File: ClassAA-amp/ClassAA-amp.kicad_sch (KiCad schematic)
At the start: 30 parts, among them J1 XH_3pin, J2 AudioJack3, J3 AudioJack3, U1 NJM4580E, U2 NJM4556

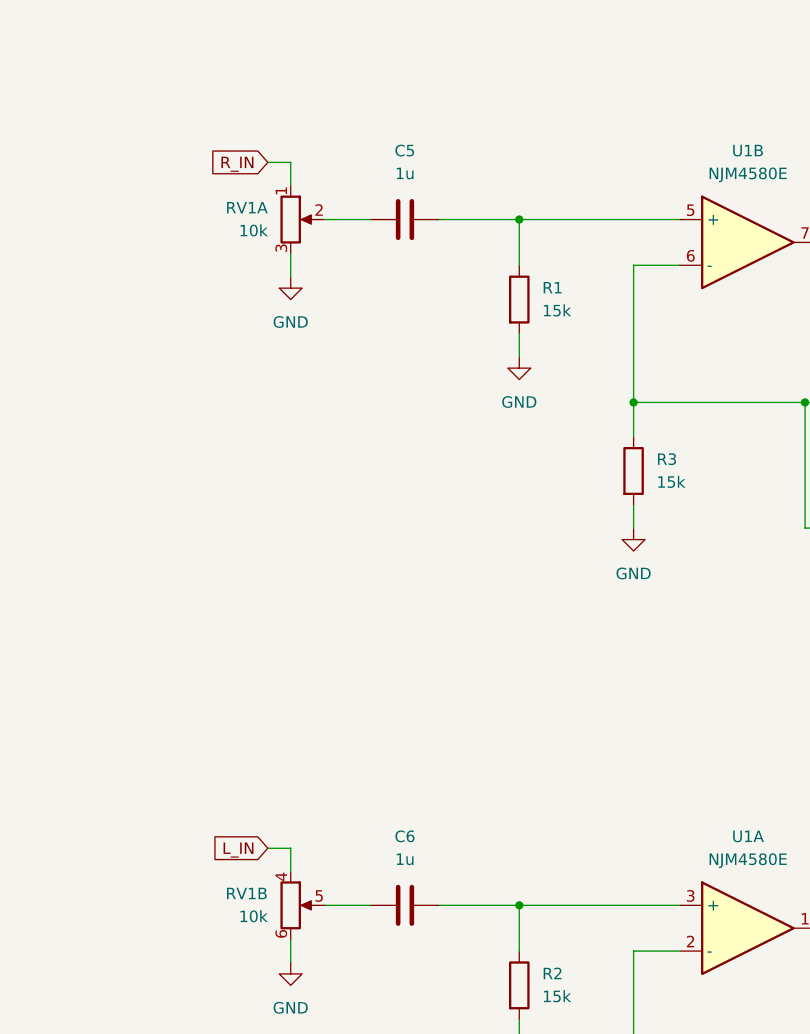
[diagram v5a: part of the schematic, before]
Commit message: 入力ハイパスフィルタのCを10uFに変更
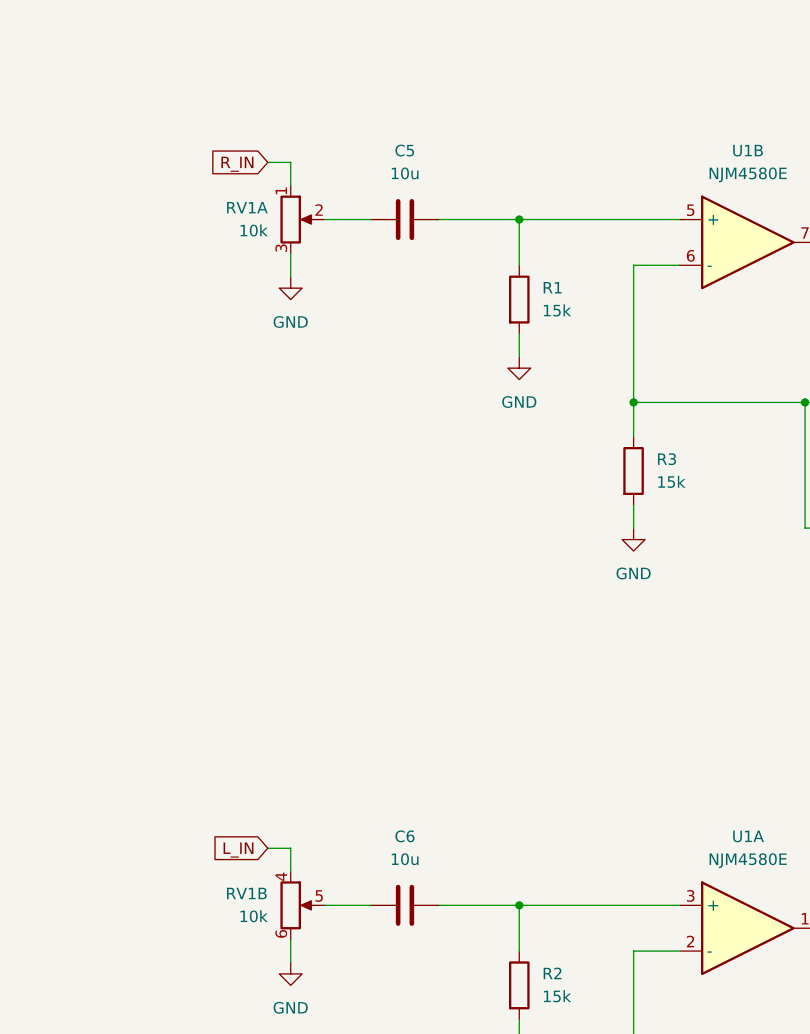
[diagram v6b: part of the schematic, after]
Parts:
- C5, C6: value 1u -> 10u
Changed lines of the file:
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@@
       (effects (font (size 1.27 1.27)))
     )
-    (property "Value" "1u" (at 139.7 119.38 90)
+    (property "Value" "10u" (at 139.7 119.38 90)
       (effects (font (size 1.27 1.27)))
     )
@@
       (effects (font (size 1.27 1.27)))
     )
-    (property "Value" "1u" (at 139.7 43.18 90)
-      (effects (font (size 1.27 1.27)))
-    )
+    (property "Value" "10u" (at 139.7 43.18 90)
+      (effects (font (size 1.27 1.27)))
+    )

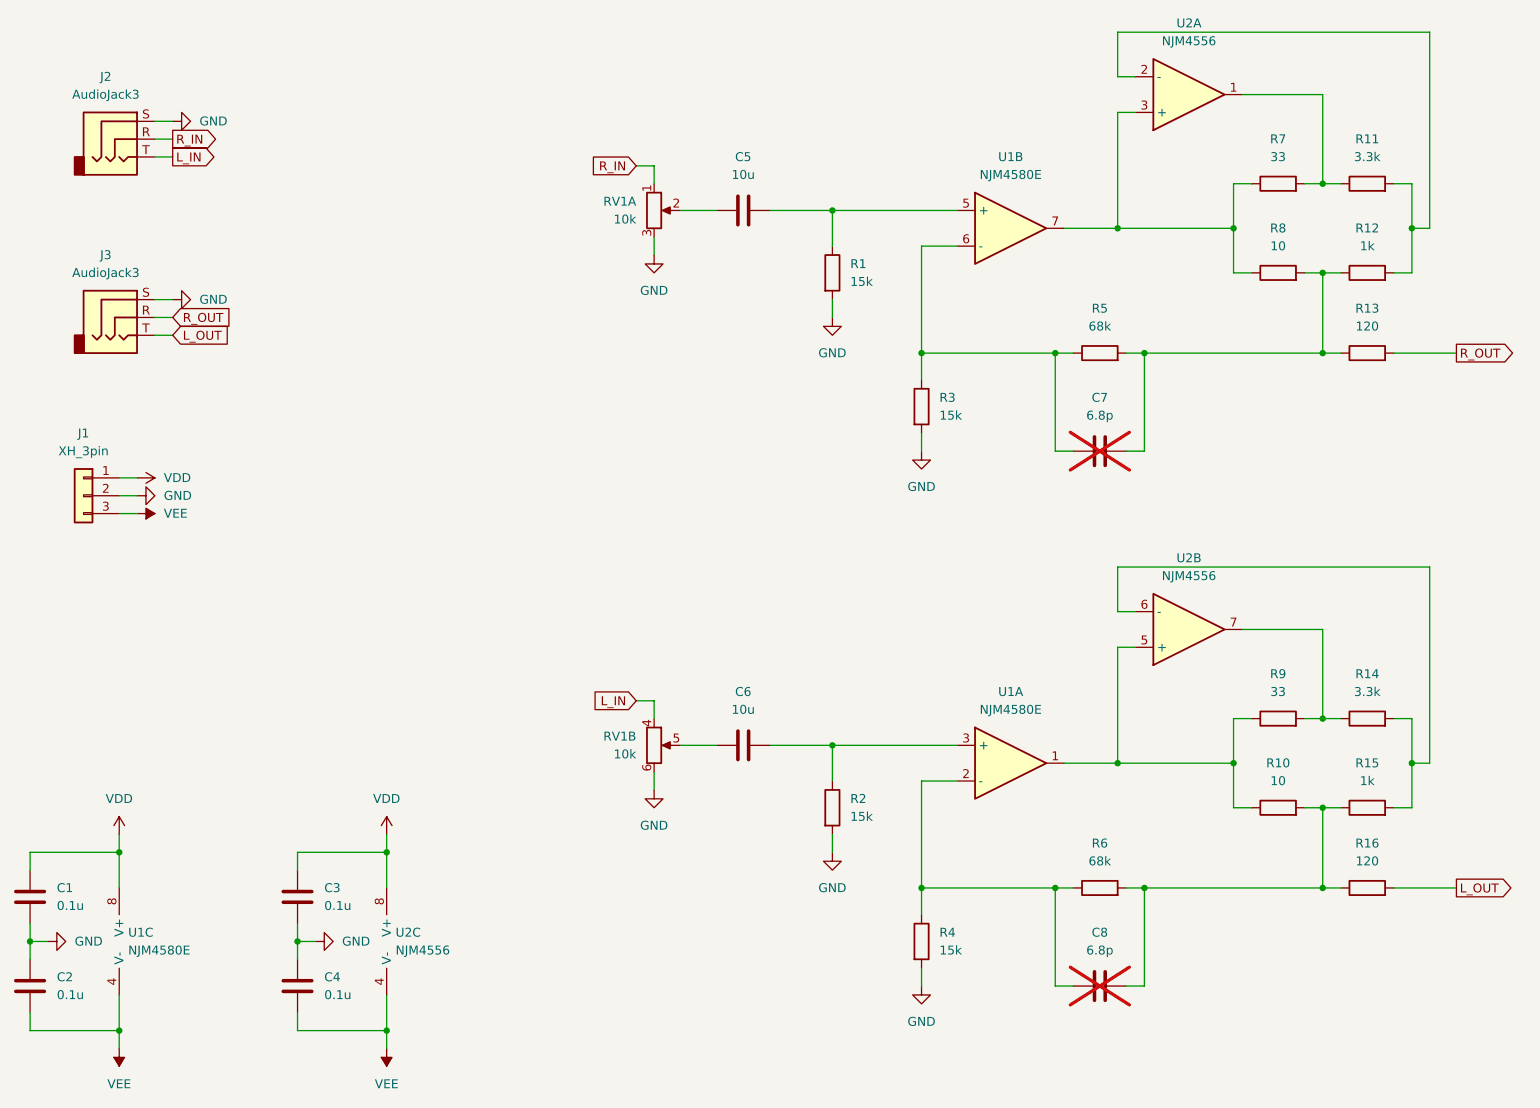
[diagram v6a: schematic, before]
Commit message: オペアンプの型番修正、フットプリント割当
NJM4580DD, NJM4556AD
フットプリントはオーディオジャック以外
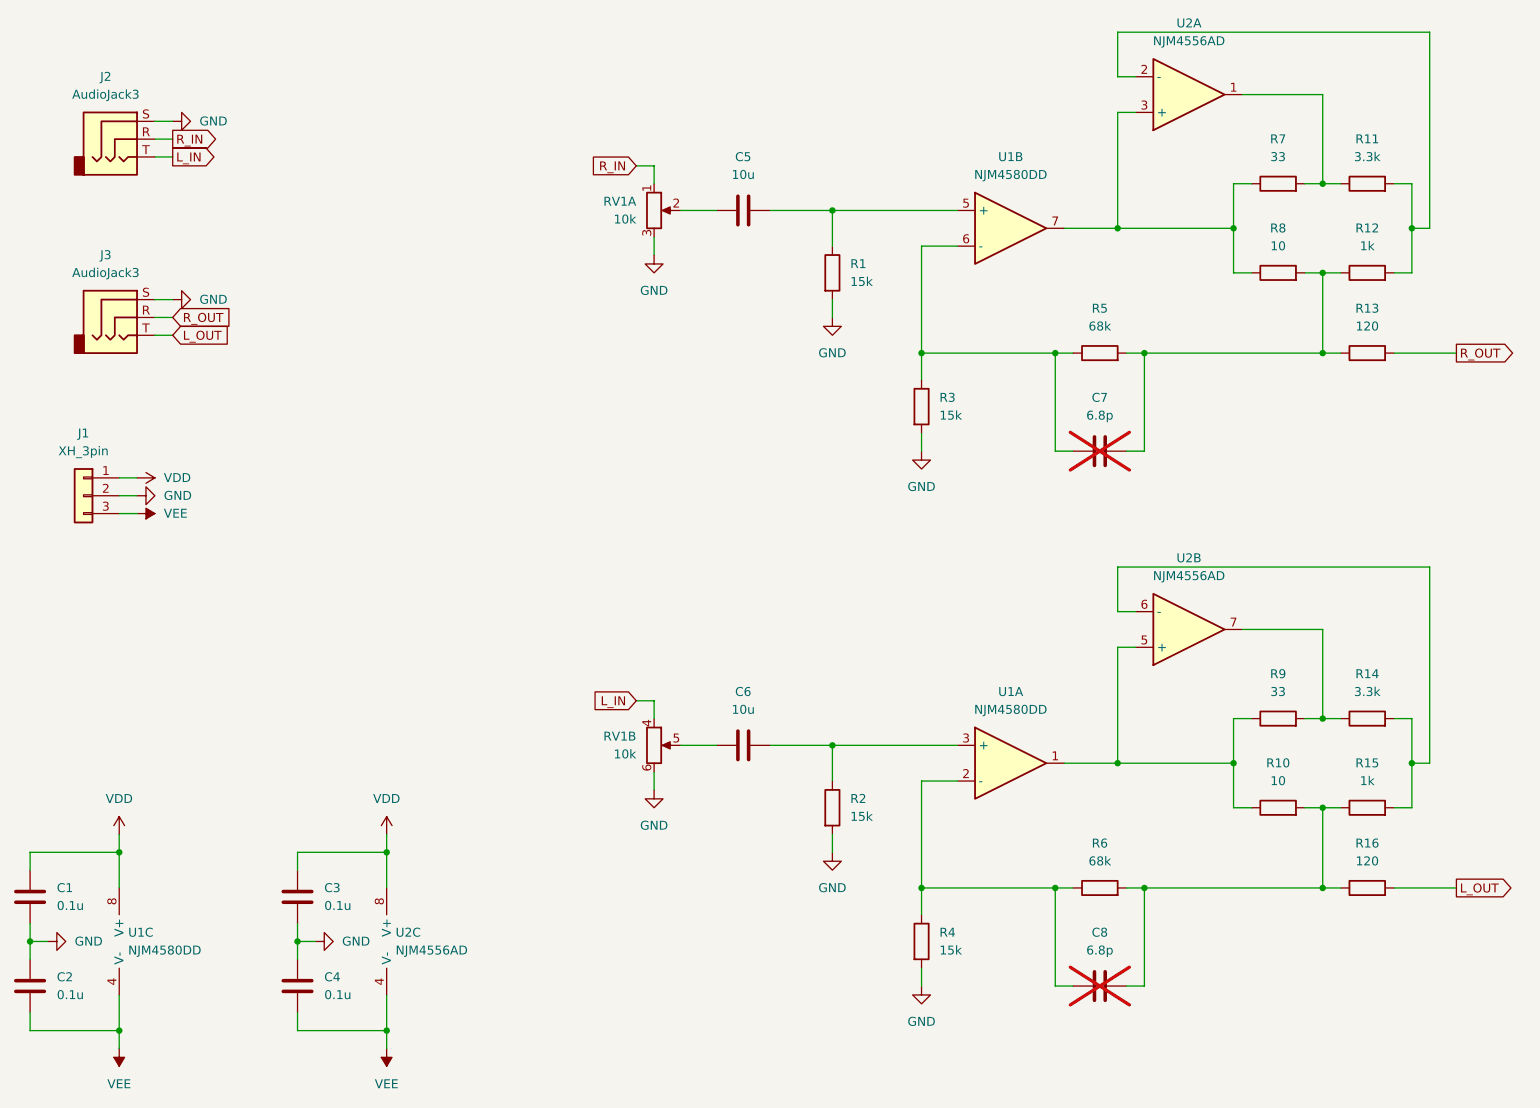
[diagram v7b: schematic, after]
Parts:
- C1, C2, C3, C4, C5, C6: footprint (none) -> Capacitor_SMD:C_0603_1608Metric
- C7, C8: footprint (none) -> Capacitor_SMD:C_0402_1005Metric
- J1: footprint (none) -> Connector_JST:JST_XH_B3B-XH-A_1x03_P2.50mm_Vertical
- R1, R10, R11, R12, R13, R14, R15, R16, R2, R3, R4, R5, R6, R7, R8, R9: footprint (none) -> Resistor_SMD:R_0603_1608Metric
- RV1: footprint (none) -> Potentiometer_THT:Potentiometer_Alps_RK097_Dual_Horizontal
- U1: value NJM4580E -> NJM4580DD; footprint (none) -> Package_DIP:DIP-8_W7.62mm_Socket
- U2: value NJM4556 -> NJM4556AD; footprint (none) -> Package_DIP:DIP-8_W7.62mm_Socket
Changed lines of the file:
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@@
       (effects (font (size 1.27 1.27)))
     )
-    (property "Footprint" "" (at 215.9 58.928 90)
+    (property "Footprint" "Resistor_SMD:R_0603_1608Metric" (at 215.9 58.928 90)
       (effects (font (size 1.27 1.27)) hide)
     )
@@
       (effects (font (size 1.27 1.27)))
     )
-    (property "Footprint" "" (at 228.6 58.928 90)
+    (property "Footprint" "Resistor_SMD:R_0603_1608Metric" (at 228.6 58.928 90)
       (effects (font (size 1.27 1.27)) hide)
     )
@@
       (effects (font (size 1.27 1.27)))
     )
-    (property "Value" "NJM4580E" (at 177.8 119.38 0)
-      (effects (font (size 1.27 1.27)))
-    )
-    (property "Footprint" "" (at 177.8 127 0)
+    (property "Value" "NJM4580DD" (at 177.8 119.38 0)
+      (effects (font (size 1.27 1.27)))
+    )
+    (property "Footprint" "Package_DIP:DIP-8_W7.62mm_Socket" (at 177.8 127 0)
       (effects (font (size 1.27 1.27)) hide)
     )
@@
       (effects (font (size 1.27 1.27)))
     )
-    (property "Footprint" "" (at 228.6 122.428 90)
+    (property "Footprint" "Resistor_SMD:R_0603_1608Metric" (at 228.6 122.428 90)
       (effects (font (size 1.27 1.27)) hide)
     )
@@
       (effects (font (size 1.27 1.27)))
     )
-    (property "Value" "NJM4556" (at 203.2 24.13 0)
-      (effects (font (size 1.27 1.27)))
-    )
-    (property "Footprint" "" (at 203.2 31.75 0)
+    (property "Value" "NJM4556AD" (at 203.2 24.13 0)
+      (effects (font (size 1.27 1.27)))
+    )
+    (property "Footprint" "Package_DIP:DIP-8_W7.62mm_Socket" (at 203.2 31.75 0)
       (effects (font (size 1.27 1.27)) hide)
     )
@@
       (effects (font (size 1.27 1.27)))
     )
-    (property "Value" "NJM4556" (at 203.2 100.33 0)
-      (effects (font (size 1.27 1.27)))
-    )
-    (property "Footprint" "" (at 203.2 107.95 0)
+    (property "Value" "NJM4556AD" (at 203.2 100.33 0)
+      (effects (font (size 1.27 1.27)))
+    )
+    (property "Footprint" "Package_DIP:DIP-8_W7.62mm_Socket" (at 203.2 107.95 0)
       (effects (font (size 1.27 1.27)) hide)
     )
@@
       (effects (font (size 1.27 1.27)) (justify left))
     )
-    (property "Footprint" "" (at 163.322 152.4 90)
+    (property "Footprint" "Resistor_SMD:R_0603_1608Metric" (at 163.322 152.4 90)
       (effects (font (size 1.27 1.27)) hide)
     )
@@
       (effects (font (size 1.27 1.27)) (justify left))
     )
-    (property "Footprint" "" (at 77.1652 149.86 0)
+    (property "Footprint" "Capacitor_SMD:C_0603_1608Metric" (at 77.1652 149.86 0)
       (effects (font (size 1.27 1.27)) hide)
     )
@@
       (effects (font (size 1.27 1.27)))
     )
-    (property "Footprint" "" (at 143.51 123.4948 0)
+    (property "Footprint" "Capacitor_SMD:C_0603_1608Metric" (at 143.51 123.4948 0)
       (effects (font (size 1.27 1.27)) hide)
     )
@@
       (effects (font (size 1.27 1.27)) (justify left))
     )
-    (property "Value" "NJM4556" (at 90.17 153.67 0)
-      (effects (font (size 1.27 1.27)) (justify left))
-    )
-    (property "Footprint" "" (at 91.44 152.4 0)
+    (property "Value" "NJM4556AD" (at 90.17 153.67 0)
+      (effects (font (size 1.27 1.27)) (justify left))
+    )
+    (property "Footprint" "Package_DIP:DIP-8_W7.62mm_Socket" (at 91.44 152.4 0)
       (effects (font (size 1.27 1.27)) hide)
     )
@@
       (effects (font (size 1.27 1.27)))
     )
-    (property "Value" "NJM4580E" (at 177.8 43.18 0)
-      (effects (font (size 1.27 1.27)))
-    )
-    (property "Footprint" "" (at 177.8 50.8 0)
+    (property "Value" "NJM4580DD" (at 177.8 43.18 0)
+      (effects (font (size 1.27 1.27)))
+    )
+    (property "Footprint" "Package_DIP:DIP-8_W7.62mm_Socket" (at 177.8 50.8 0)
       (effects (font (size 1.27 1.27)) hide)
     )
@@
       (effects (font (size 1.27 1.27)) (justify left))
     )
-    (property "Footprint" "" (at 39.0652 149.86 0)
+    (property "Footprint" "Capacitor_SMD:C_0603_1608Metric" (at 39.0652 149.86 0)
       (effects (font (size 1.27 1.27)) hide)
     )
@@
       (effects (font (size 1.27 1.27)) (justify left))
     )
-    (property "Footprint" "" (at 39.0652 162.56 0)
+    (property "Footprint" "Capacitor_SMD:C_0603_1608Metric" (at 39.0652 162.56 0)
       (effects (font (size 1.27 1.27)) hide)
     )
@@
       (effects (font (size 1.27 1.27)))
     )
-    (property "Footprint" "" (at 143.51 47.2948 0)
+    (property "Footprint" "Capacitor_SMD:C_0603_1608Metric" (at 143.51 47.2948 0)
       (effects (font (size 1.27 1.27)) hide)
     )
@@
       (effects (font (size 1.27 1.27)) (justify right))
     )
-    (property "Footprint" "" (at 127 124.46 0)
+    (property "Footprint" "Potentiometer_THT:Potentiometer_Alps_RK097_Dual_Horizontal" (at 127 124.46 0)
       (effects (font (size 1.27 1.27)) hide)
     )
@@
       (effects (font (size 1.27 1.27)))
     )
-    (property "Footprint" "" (at 228.6 135.128 90)
+    (property "Footprint" "Resistor_SMD:R_0603_1608Metric" (at 228.6 135.128 90)
       (effects (font (size 1.27 1.27)) hide)
     )
@@
       (effects (font (size 1.27 1.27)))
     )
-    (property "Footprint" "" (at 190.5 146.558 90)
+    (property "Footprint" "Resistor_SMD:R_0603_1608Metric" (at 190.5 146.558 90)
       (effects (font (size 1.27 1.27)) hide)
     )
@@
       (effects (font (size 1.27 1.27)) (justify left))
     )
-    (property "Footprint" "" (at 150.622 57.15 90)
+    (property "Footprint" "Resistor_SMD:R_0603_1608Metric" (at 150.622 57.15 90)
       (effects (font (size 1.27 1.27)) hide)
     )
@@
       (effects (font (size 1.27 1.27)))
     )
-    (property "Footprint" "" (at 45.72 88.9 0)
+    (property "Footprint" "Connector_JST:JST_XH_B3B-XH-A_1x03_P2.50mm_Vertical" (at 45.72 88.9 0)
       (effects (font (size 1.27 1.27)) hide)
     )
@@
       (effects (font (size 1.27 1.27)))
     )
-    (property "Footprint" "" (at 194.31 157.7848 0)
+    (property "Footprint" "Capacitor_SMD:C_0402_1005Metric" (at 194.31 157.7848 0)
       (effects (font (size 1.27 1.27)) hide)
     )
@@
       (effects (font (size 1.27 1.27)) (justify left))
     )
-    (property "Value" "NJM4580E" (at 52.07 153.67 0)
-      (effects (font (size 1.27 1.27)) (justify left))
-    )
-    (property "Footprint" "" (at 53.34 152.4 0)
+    (property "Value" "NJM4580DD" (at 52.07 153.67 0)
+      (effects (font (size 1.27 1.27)) (justify left))
+    )
+    (property "Footprint" "Package_DIP:DIP-8_W7.62mm_Socket" (at 53.34 152.4 0)
       (effects (font (size 1.27 1.27)) hide)
     )
@@
       (effects (font (size 1.27 1.27)))
     )
-    (property "Footprint" "" (at 190.5 70.358 90)
+    (property "Footprint" "Resistor_SMD:R_0603_1608Metric" (at 190.5 70.358 90)
       (effects (font (size 1.27 1.27)) hide)
     )
@@
       (effects (font (size 1.27 1.27)))
     )
-    (property "Footprint" "" (at 228.6 46.228 90)
+    (property "Footprint" "Resistor_SMD:R_0603_1608Metric" (at 228.6 46.228 90)
       (effects (font (size 1.27 1.27)) hide)
     )
@@
       (effects (font (size 1.27 1.27)))
     )
-    (property "Footprint" "" (at 215.9 46.228 90)
+    (property "Footprint" "Resistor_SMD:R_0603_1608Metric" (at 215.9 46.228 90)
       (effects (font (size 1.27 1.27)) hide)
     )
@@
       (effects (font (size 1.27 1.27)))
     )
-    (property "Footprint" "" (at 228.6 146.558 90)
+    (property "Footprint" "Resistor_SMD:R_0603_1608Metric" (at 228.6 146.558 90)
       (effects (font (size 1.27 1.27)) hide)
     )
@@
       (effects (font (size 1.27 1.27)) (justify left))
     )
-    (property "Footprint" "" (at 150.622 133.35 90)
+    (property "Footprint" "Resistor_SMD:R_0603_1608Metric" (at 150.622 133.35 90)
       (effects (font (size 1.27 1.27)) hide)
     )
@@
       (effects (font (size 1.27 1.27)) (justify left))
     )
-    (property "Footprint" "" (at 163.322 76.2 90)
+    (property "Footprint" "Resistor_SMD:R_0603_1608Metric" (at 163.322 76.2 90)
       (effects (font (size 1.27 1.27)) hide)
     )
@@
       (effects (font (size 1.27 1.27)))
     )
-    (property "Footprint" "" (at 215.9 135.128 90)
+    (property "Footprint" "Resistor_SMD:R_0603_1608Metric" (at 215.9 135.128 90)
       (effects (font (size 1.27 1.27)) hide)
     )
@@
       (effects (font (size 1.27 1.27)) (justify left))
     )
-    (property "Footprint" "" (at 77.1652 162.56 0)
+    (property "Footprint" "Capacitor_SMD:C_0603_1608Metric" (at 77.1652 162.56 0)
       (effects (font (size 1.27 1.27)) hide)
     )
@@
       (effects (font (size 1.27 1.27)) (justify right))
     )
-    (property "Footprint" "" (at 127 48.26 0)
+    (property "Footprint" "Potentiometer_THT:Potentiometer_Alps_RK097_Dual_Horizontal" (at 127 48.26 0)
       (effects (font (size 1.27 1.27)) hide)
     )
@@
       (effects (font (size 1.27 1.27)))
     )
-    (property "Footprint" "" (at 194.31 81.5848 0)
+    (property "Footprint" "Capacitor_SMD:C_0402_1005Metric" (at 194.31 81.5848 0)
       (effects (font (size 1.27 1.27)) hide)
     )
@@
       (effects (font (size 1.27 1.27)))
     )
-    (property "Footprint" "" (at 228.6 70.358 90)
+    (property "Footprint" "Resistor_SMD:R_0603_1608Metric" (at 228.6 70.358 90)
       (effects (font (size 1.27 1.27)) hide)
     )
@@
       (effects (font (size 1.27 1.27)))
     )
-    (property "Footprint" "" (at 215.9 122.428 90)
-      (effects (font (size 1.27 1.27)) hide)
-    )
+    (property "Footprint" "Resistor_SMD:R_0603_1608Metric" (at 215.9 122.428 90)
+      (effects (font (size 1.27 1.27)) hide)
+    )

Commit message: オーディオジャックのフットプリント割当
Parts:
- J2, J3: footprint (none) -> Connector_Audio:Jack_3.5mm_Switronic_ST-005-G_horizontal
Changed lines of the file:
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@@
       (effects (font (size 1.27 1.27)))
     )
-    (property "Footprint" "" (at 50.8 38.1 0)
+    (property "Footprint" "Connector_Audio:Jack_3.5mm_Switronic_ST-005-G_horizontal" (at 50.8 38.1 0)
       (effects (font (size 1.27 1.27)) hide)
     )
@@
       (effects (font (size 1.27 1.27)))
     )
-    (property "Footprint" "" (at 50.8 63.5 0)
+    (property "Footprint" "Connector_Audio:Jack_3.5mm_Switronic_ST-005-G_horizontal" (at 50.8 63.5 0)
       (effects (font (size 1.27 1.27)) hide)
     )
